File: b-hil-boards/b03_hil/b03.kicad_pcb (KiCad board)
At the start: 2 copper layers, 100 x 50 mm, 57 parts, among them J1 Conn_01x20_Socket, J2 Conn_01x14_Socket, K1 Relay_DPDT, K2 Relay_DPDT, K3 Relay_DPDT, K4 Relay_DPDT, K5 Relay_DPDT, K6 Relay_DPDT, SW1 SW_Push, U1 74LVC2G34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

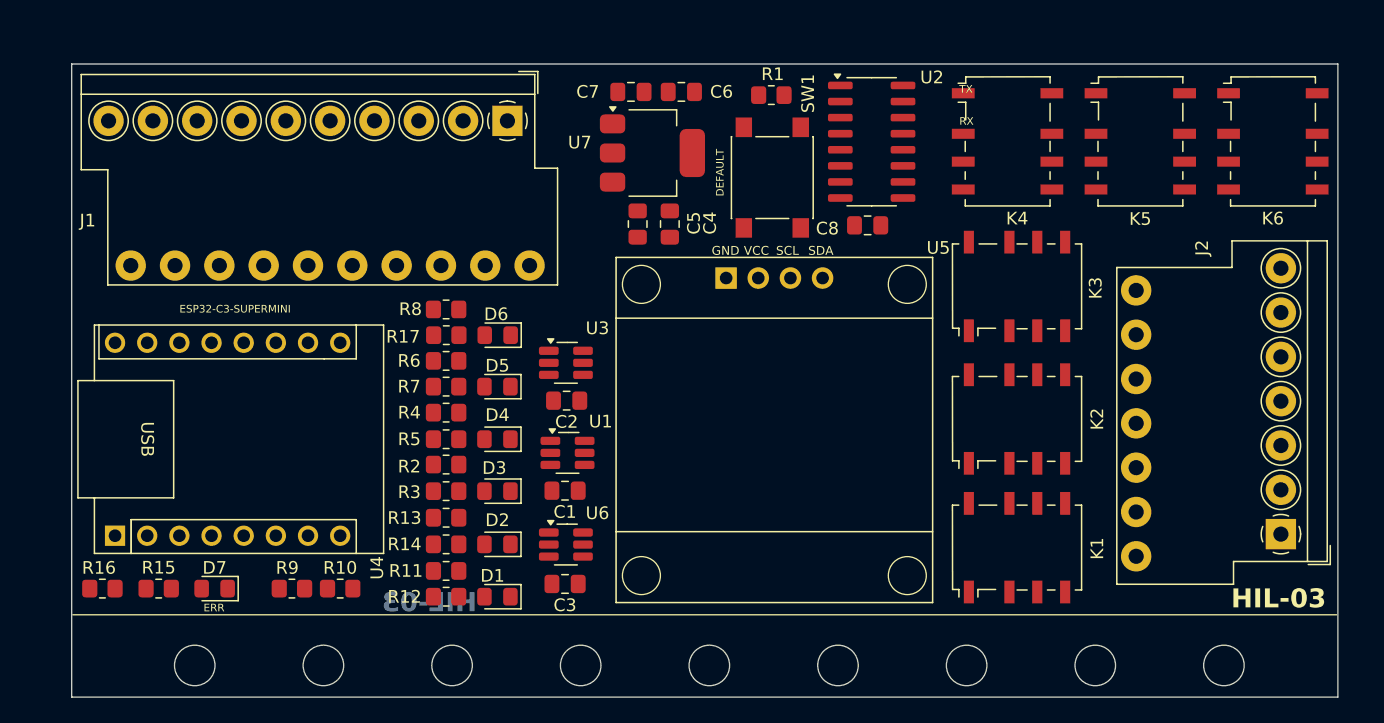
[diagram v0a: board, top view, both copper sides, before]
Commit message: B03: route all board traces
- Complete trace routing for B03 HIL board
- Update PCB layout (b03.kicad_pcb) and schematic (b03.kicad_sch)
- Add routing session/export files and backups
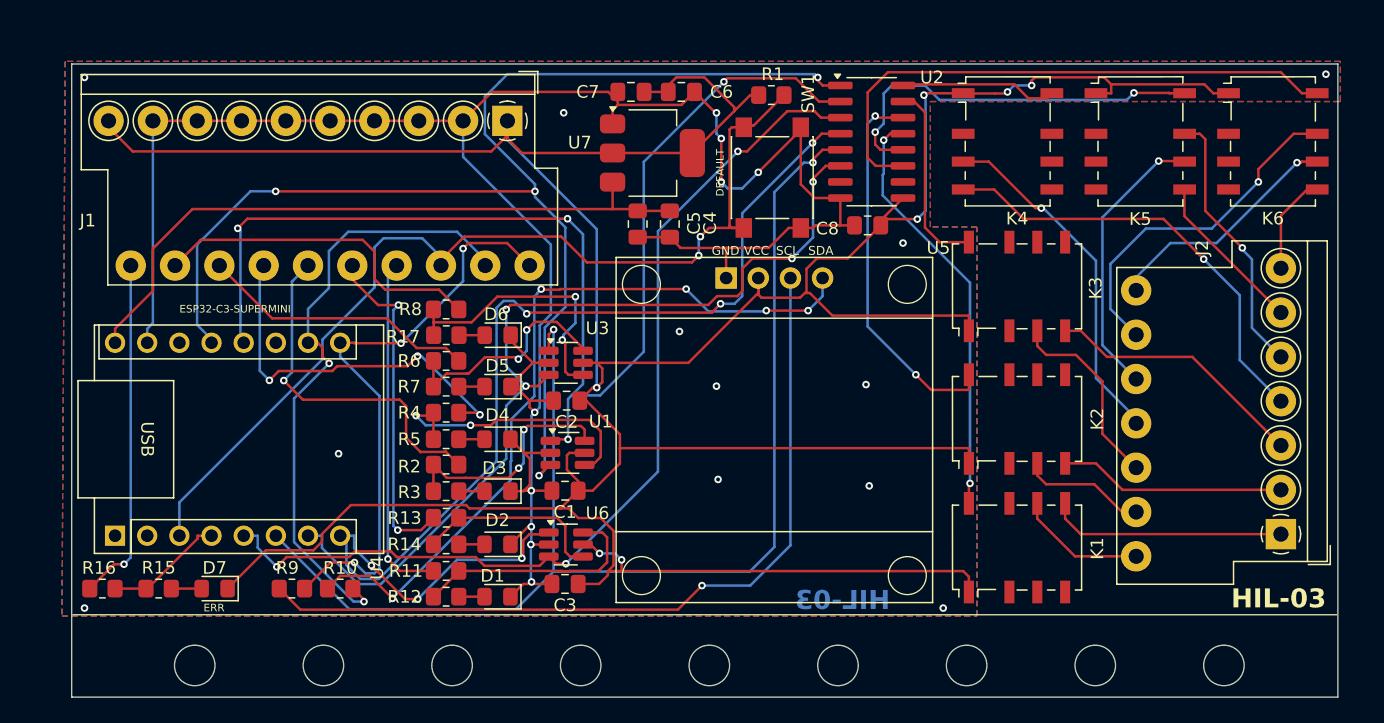
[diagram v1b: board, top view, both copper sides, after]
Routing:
- net +3V3: track 0.00 -> 306.7 mm, vias 0 -> 7
- net GND: track 0.00 -> 181.7 mm, vias 0 -> 21
- net /K4CTR: track 0.00 -> 100.6 mm, vias 0 -> 4
- net /K5CTR: track 0.00 -> 99.5 mm, vias 0 -> 2
- net /K3CTR: track 0.00 -> 96.6 mm, vias 0 -> 4
- net /K1CTR: track 0.00 -> 90.2 mm, vias 0 -> 6
- net /DEFAULTS: track 0.00 -> 78.1 mm, vias 0 -> 2
- net /K2CTR: track 0.00 -> 76.3 mm, vias 0 -> 3
- net /K6CTR: track 0.00 -> 72.0 mm, vias 0 -> 4
- net Net-(U5-SCL): track 0.00 -> 64.3 mm, vias 0 -> 1
- net Net-(U5-SDA): track 0.00 -> 60.5 mm, vias 0 -> 5
- net +5V: track 0.00 -> 53.0 mm
- net /DISP_SDA: track 0.00 -> 49.2 mm, vias 0 -> 2
- net /DISP_SCL: track 0.00 -> 46.9 mm, vias 0 -> 3
- net Net-(U2-O6): track 0.00 -> 45.1 mm
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- added copper zone on B.Cu, net GND
- added copper zone on F.Cu, net GND
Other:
- board text added: "K1C"
- board text added: "K1NO"
- board text added: "K2C"
- board text added: "K2NO"
- board text added: "K3C"
- board text added: "K3NO"
- board text added: "K4C"
- board text added: "K4NO"
- board text added: "K5C"
- board text added: "K5NC"
- board text added: "K5NO"
- board text added: "K6C"
- board text added: "K6NC"
- board text added: "K6NO"
- board text removed: "RX"
- board text removed: "TX"

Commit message: B03: add Gerber output for single board
- Create Gerber files for single-board fabrication (gerber/single/)
- Include copper, mask, paste, silkscreen, edge cuts and drill files
- Add b03-single.zip package for manufacturer
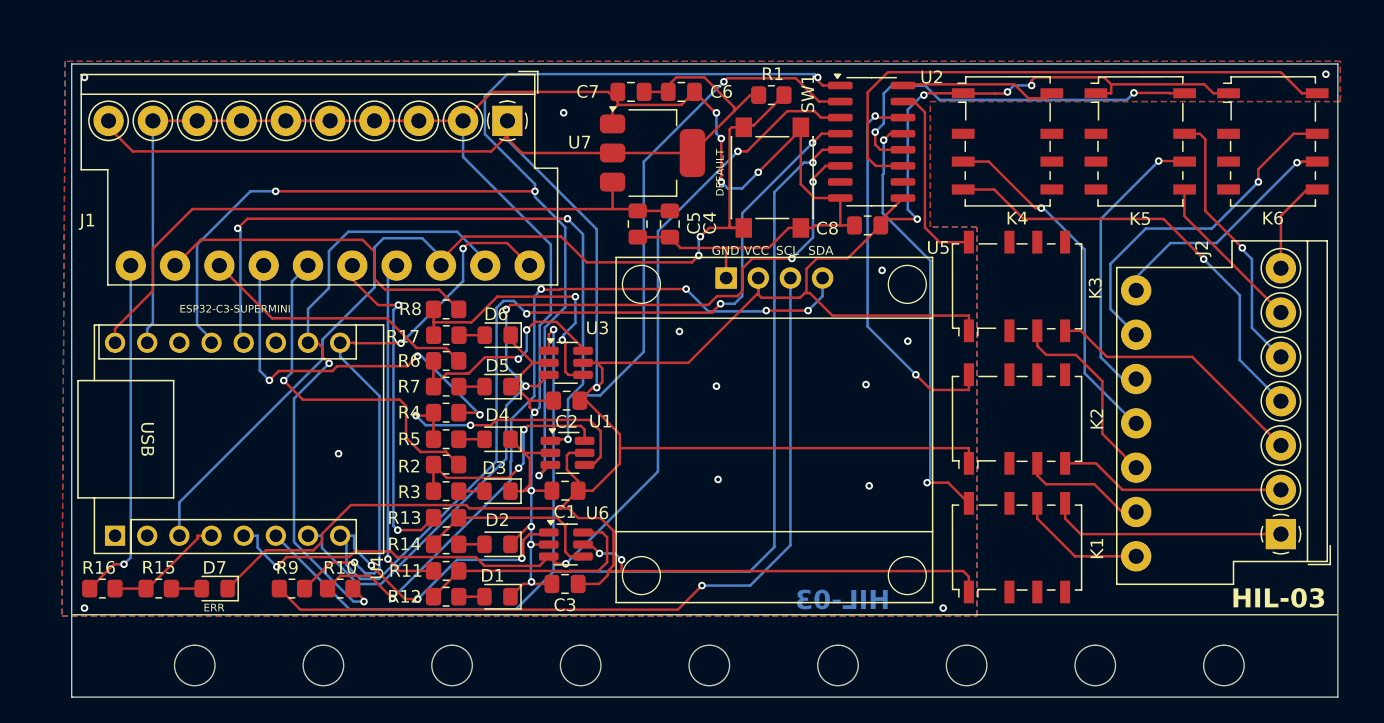
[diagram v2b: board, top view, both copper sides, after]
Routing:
- net Net-(U2-O4): track 33.7 -> 34.9 mm
- net /K5C: track 22.2 -> 23.0 mm
- net +3V3: track 306.7 -> 307.3 mm
- net GND: vias 21 -> 22

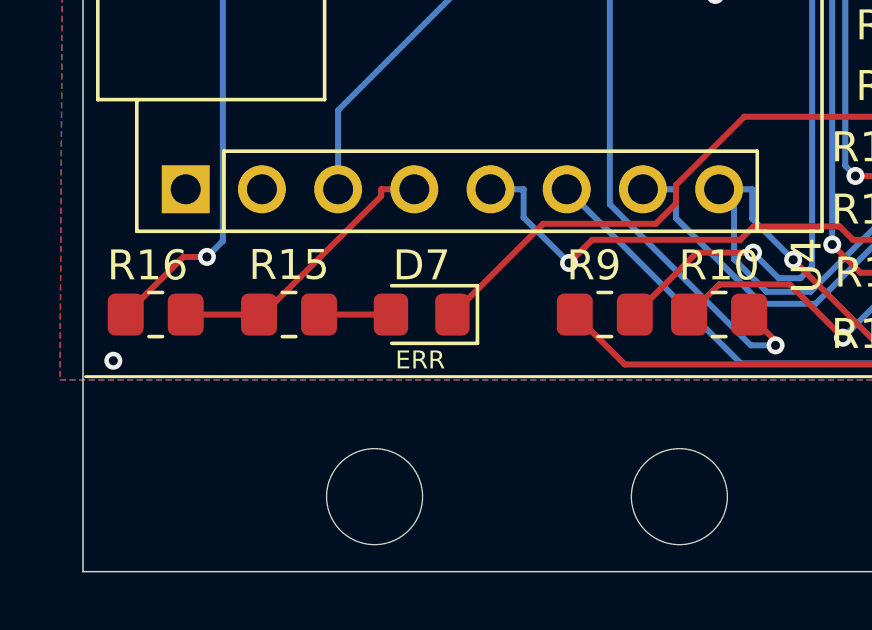
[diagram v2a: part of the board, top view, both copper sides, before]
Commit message: fix(b03): correct LED D7 polarity on schematic and PCB
Fix reversed polarity marking/connection for D7 in b03.kicad_sch and
b03.kicad_pcb.
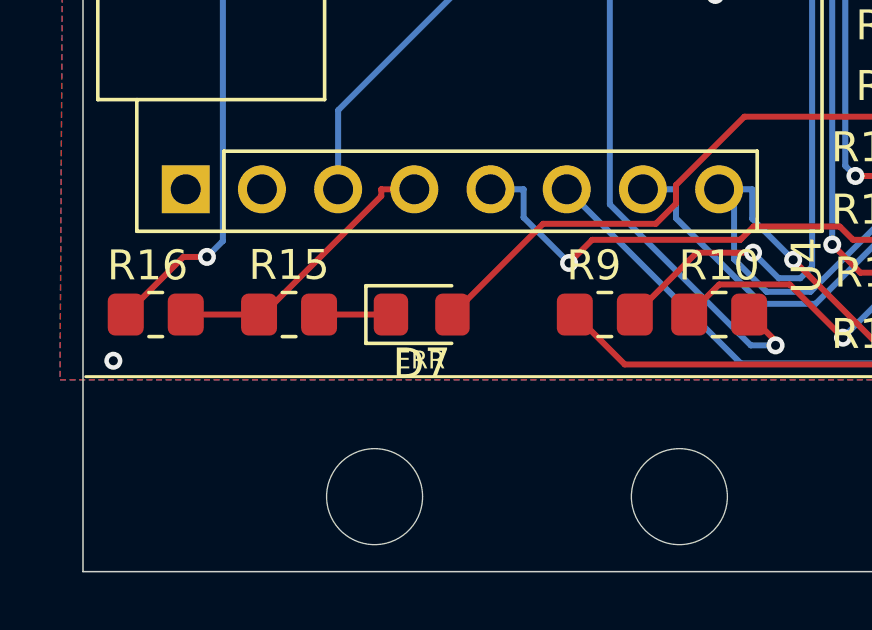
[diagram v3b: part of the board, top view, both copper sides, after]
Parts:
- turned D7 to 0 degrees
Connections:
- D7 pad 1: +3V3 -> Net-(D7-K)
- D7 pad 2: Net-(D7-A) -> +3V3
- R15 pad 2: Net-(D7-A) -> Net-(D7-K)
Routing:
- net Net-(D7-K): track 0.00 -> 2.40 mm
- net Net-(D7-A): track 2.40 -> 0.00 mm
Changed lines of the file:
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@@
   (net 49 "unconnected-(U4-GPIO6-Pad2)")
   (net 50 "Net-(D6-A)")
-  (net 51 "Net-(D7-A)")
+  (net 51 "Net-(D7-K)")
   (net 52 "/K6C")
   (net 53 "/K6NO")
@@
   )
   (footprint "LED_SMD:LED_0805_2012Metric_Pad1.15x1.40mm_HandSolder" (layer "F.Cu")
-    (at 91.05 75.93 180)
+    (at 91.05 75.93)
     (descr "LED SMD 0805 (2012 Metric), square (rectangular) end terminal, IPC_7351 nominal, (Body size source: https://docs.google.com/spreadsheets/d/1BsfQQcO9C6DZCsRaXUlFlo91Tg2WpOkGARC1WS5S8t0/edit?usp=sharing), generated with kicad-footprint-generator")
     (tags "LED handsolder")
@@
     (fp_line (start 1 0.6) (end 1 -0.6)
       (stroke (width 0.1) (type solid)) (layer "F.Fab"))
-    (pad "1" smd roundrect (at -1.025 0 180) (size 1.15 1.4) (layers "F.Cu" "F.Paste" "F.Mask") (roundrect_rratio 0.2173913043)
-      (net 2 "+3V3") (pinfunction "K") (pintype "passive"))
-    (pad "2" smd roundrect (at 1.025 0 180) (size 1.15 1.4) (layers "F.Cu" "F.Paste" "F.Mask") (roundrect_rratio 0.2173913043)
-      (net 51 "Net-(D7-A)") (pinfunction "A") (pintype "passive"))
+    (pad "1" smd roundrect (at -1.025 0) (size 1.15 1.4) (layers "F.Cu" "F.Paste" "F.Mask") (roundrect_rratio 0.2173913043)
+      (net 51 "Net-(D7-K)") (pinfunction "K") (pintype "passive"))
+    (pad "2" smd roundrect (at 1.025 0) (size 1.15 1.4) (layers "F.Cu" "F.Paste" "F.Mask") (roundrect_rratio 0.2173913043)
+      (net 2 "+3V3") (pinfunction "A") (pintype "passive"))
     (model "${KICAD6_3DMODEL_DIR}/LED_SMD.3dshapes/LED_0805_2012Metric.wrl"
       (offset (xyz 0 0 0))
@@
       (net 41 "/ERR_LED") (pintype "passive"))
     (pad "2" smd roundrect (at 1 0) (size 1.2 1.4) (layers "F.Cu" "F.Paste" "F.Mask") (roundrect_rratio 0.2083333333)
-      (net 51 "Net-(D7-A)") (pintype "passive"))
+      (net 51 "Net-(D7-K)") (pintype "passive"))
     (model "${KICAD6_3DMODEL_DIR}/Resistor_SMD.3dshapes/R_0805_2012Metric.wrl"
       (offset (xyz 0 0 0))

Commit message: B02: invert UART indicator LED polarity; refresh KiCad backups
- B02: reflect UART status LED polarity in schematic and PCB; update project layout.
- B02/B03/B04: rotate KiCad automatic backup zips (remove obsolete B02 backups, add current ones).
- B03: tweak D7 silkscreen/Fab text offsets on PCB (reference and value placement).
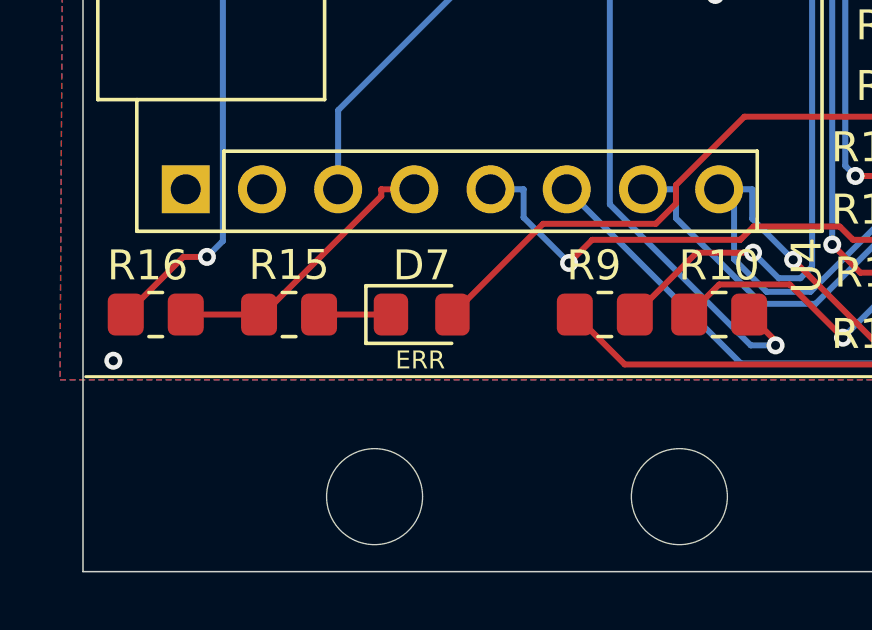
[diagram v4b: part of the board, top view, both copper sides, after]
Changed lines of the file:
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@@
     (property "ki_keywords" "LED diode")
     (attr smd)
-    (fp_text reference "D7" (at 0 1.635) (layer "F.SilkS")
+    (fp_text reference "D7" (at 0 -1.635) (layer "F.SilkS")
         (effects (font (size 1 1) (thickness 0.15)))
     )
-    (fp_text value "LED" (at 0 1.65) (layer "F.Fab")
+    (fp_text value "LED" (at 0 -1.635) (layer "F.Fab")
         (effects (font (size 1 1) (thickness 0.15)))
     )

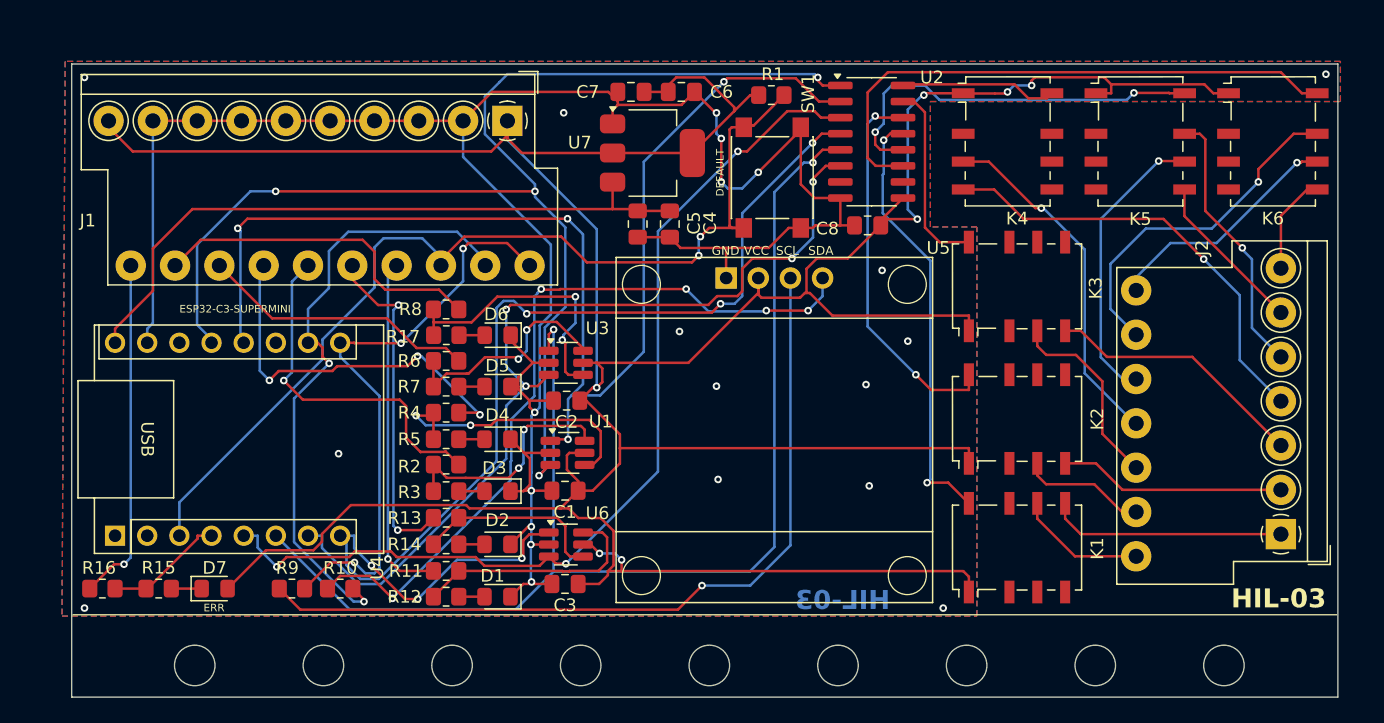
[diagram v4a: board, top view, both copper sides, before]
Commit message: B03: add tri-state buffer and re-route PCB
Add 74HCT541 tri-state buffer to the schematic and re-route b03.kicad_pcb
to integrate the new device. Update project settings, replace FreeRouting
exchange files (b03.dsn, b03.rules, b03.ses; remove legacy b02.*), and
rotate KiCad automatic backup archives.
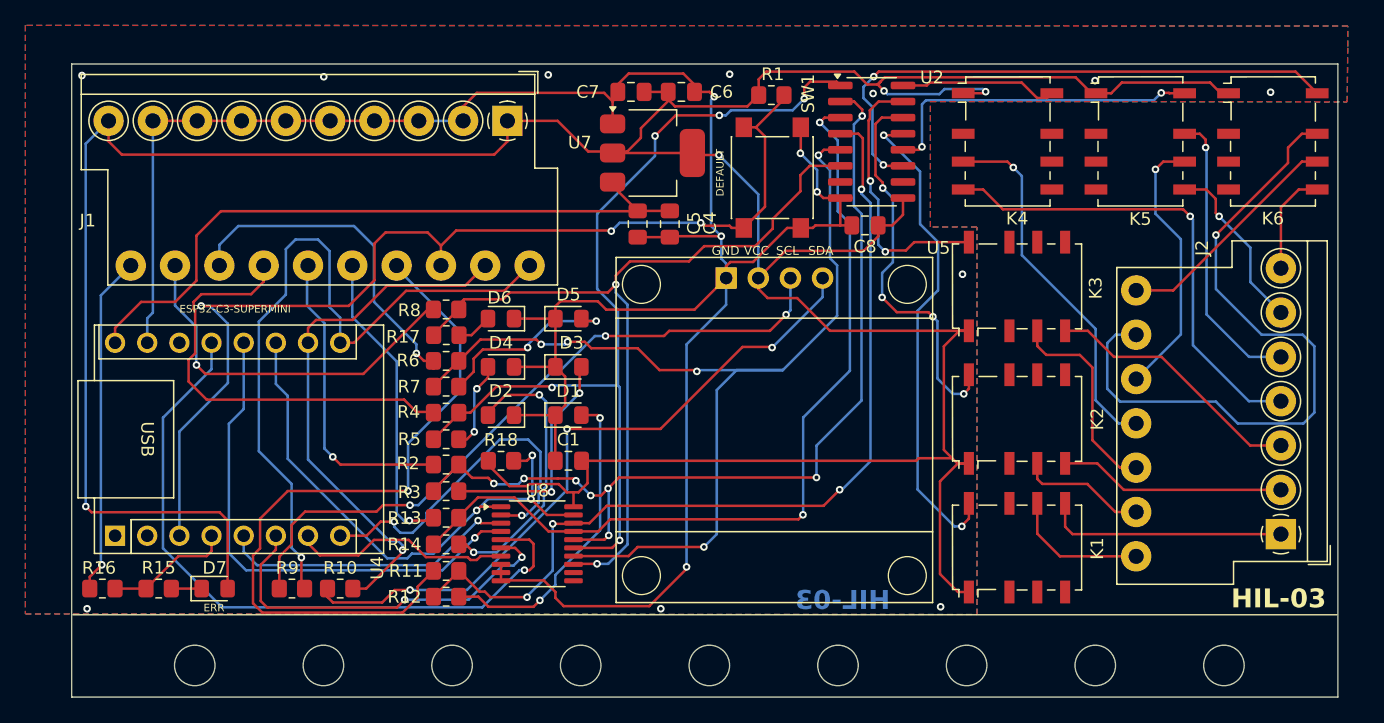
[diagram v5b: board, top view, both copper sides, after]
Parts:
- removed C2, C3: C, Capacitor_SMD:C_0805_2012Metric_Pad1.18x1.45mm_HandSolder
- removed U1, U3, U6: 74LVC2G34, Package_TO_SOT_SMD:SOT-23-6_Handsoldering
- added R18: R, Resistor_SMD:R_0805_2012Metric_Pad1.20x1.40mm_HandSolder, F.Cu at (113.7, 65.8)
- added U8: 74HCT541, Package_SO:TSSOP-20_4.4x6.5mm_P0.65mm, F.Cu at (116.5, 72.4)
- moved D1 15.4 mm to (119.0, 62.2), turned to 0 degrees
- moved D3 11.3 mm to (119.0, 58.4), turned to 0 degrees
- moved D2 10.2 mm to (113.7, 62.2)
- moved D5 7.76 mm to (119.0, 54.6), turned to 0 degrees
- moved D4 5.72 mm to (113.7, 58.4)
- moved C1 2.38 mm to (119.0, 65.8)
- moved D6 1.33 mm to (113.7, 54.6)
- moved C8 0.21 mm to (142.4, 47.2)
- turned R2 to 180 degrees
- turned R4 to 180 degrees
- turned R6 to 180 degrees
- turned R8 to 180 degrees
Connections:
- R11 pad 1: Net-(R11-Pad1) -> /K1DRV
- R12 pad 1: Net-(R11-Pad1) -> /K1DRV
- R13 pad 1: Net-(R13-Pad1) -> /K2DRV
- R14 pad 1: Net-(R13-Pad1) -> /K2DRV
- R17 pad 1: Net-(R17-Pad1) -> /K6DRV
- R2 pad 1: Net-(R2-Pad1) -> /K3DRV
- R3 pad 1: Net-(R2-Pad1) -> /K3DRV
- R4 pad 1: Net-(R4-Pad1) -> /K4DRV
- R5 pad 1: Net-(R4-Pad1) -> /K4DRV
- R6 pad 1: Net-(R6-Pad1) -> /K5DRV
- R7 pad 1: Net-(R6-Pad1) -> /K5DRV
- R8 pad 1: Net-(R17-Pad1) -> /K6DRV
- U2 pad 1: /K4CTR -> /K4DRV
- U2 pad 2: /K3CTR -> /K3DRV
- U2 pad 3: /K2CTR -> /K2DRV
- U2 pad 4: /K1CTR -> /K1DRV
- U2 pad 5: /K5CTR -> /K5DRV
- U2 pad 6: /K6CTR -> /K6DRV
- U4 pad 11: unconnected-(U4-GPIO2-Pad11) -> //KOE
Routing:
- net /K5DRV: track 0.00 -> 81.0 mm, vias 0 -> 5
- net /K3DRV: track 0.00 -> 72.8 mm, vias 0 -> 8
- net /K4DRV: track 0.00 -> 72.0 mm, vias 0 -> 5
- net /K1DRV: track 0.00 -> 71.5 mm, vias 0 -> 4
- net /K5CTR: track 99.5 -> 30.2 mm
- net /K2DRV: track 0.00 -> 67.8 mm, vias 0 -> 2
- net /K6DRV: track 0.00 -> 65.4 mm, vias 0 -> 2
- net /K1CTR: track 90.2 -> 28.1 mm, vias 6 -> 2
- net /K3CTR: track 96.6 -> 40.4 mm, vias 4 -> 1
- net /K6CTR: track 72.0 -> 17.5 mm, vias 4 -> 0
- net /K2CTR: track 76.3 -> 23.6 mm, vias 3 -> 1
- net /K4CTR: track 100.6 -> 54.8 mm, vias 4 -> 1
- net //KOE: track 0.00 -> 45.0 mm, vias 0 -> 3
- net /K1_LED_EXT: track 27.4 -> 57.5 mm
- net /K6NC: track 27.6 -> 55.2 mm
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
